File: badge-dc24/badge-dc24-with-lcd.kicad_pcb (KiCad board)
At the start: 2 copper layers, 22 parts, among them P1 CONN_01X02, U1 ESP-12E, U2 TSOP38238, U3 74HC595

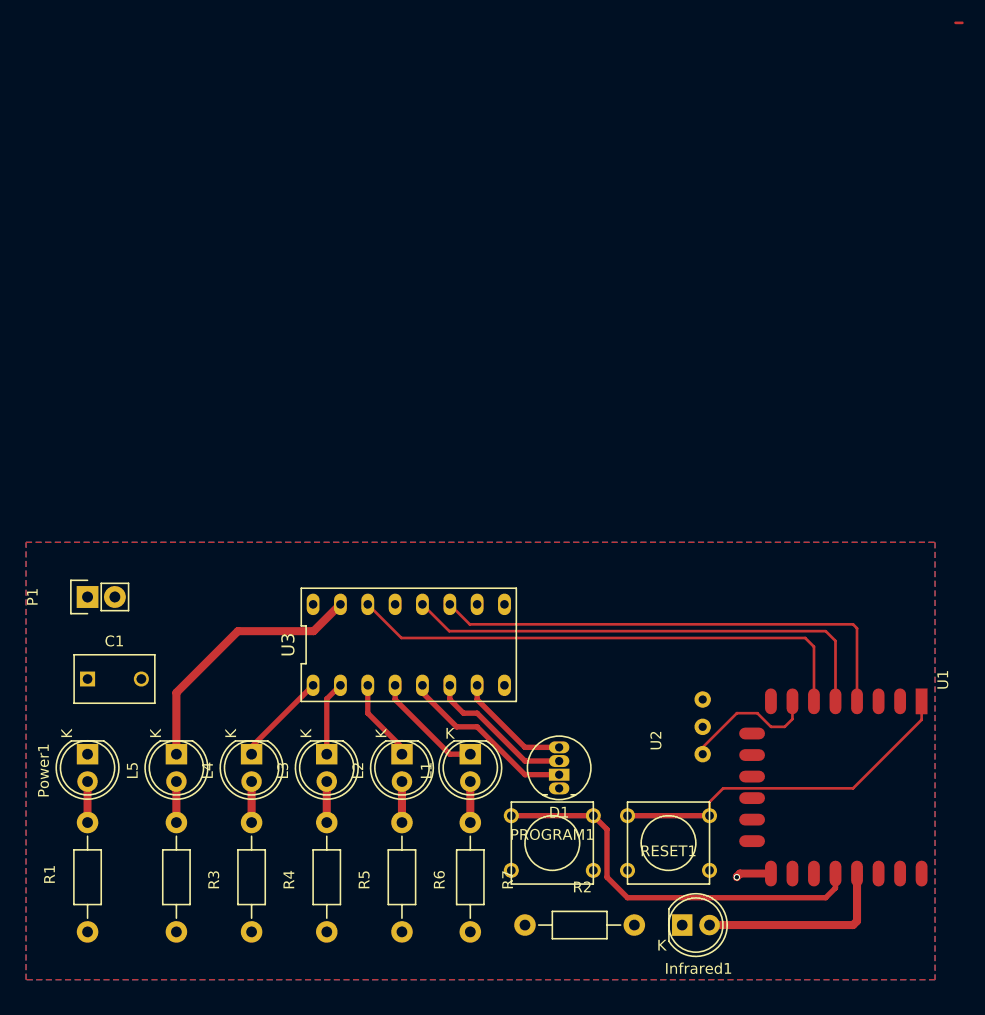
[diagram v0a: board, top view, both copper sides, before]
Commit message: SMD fir some components
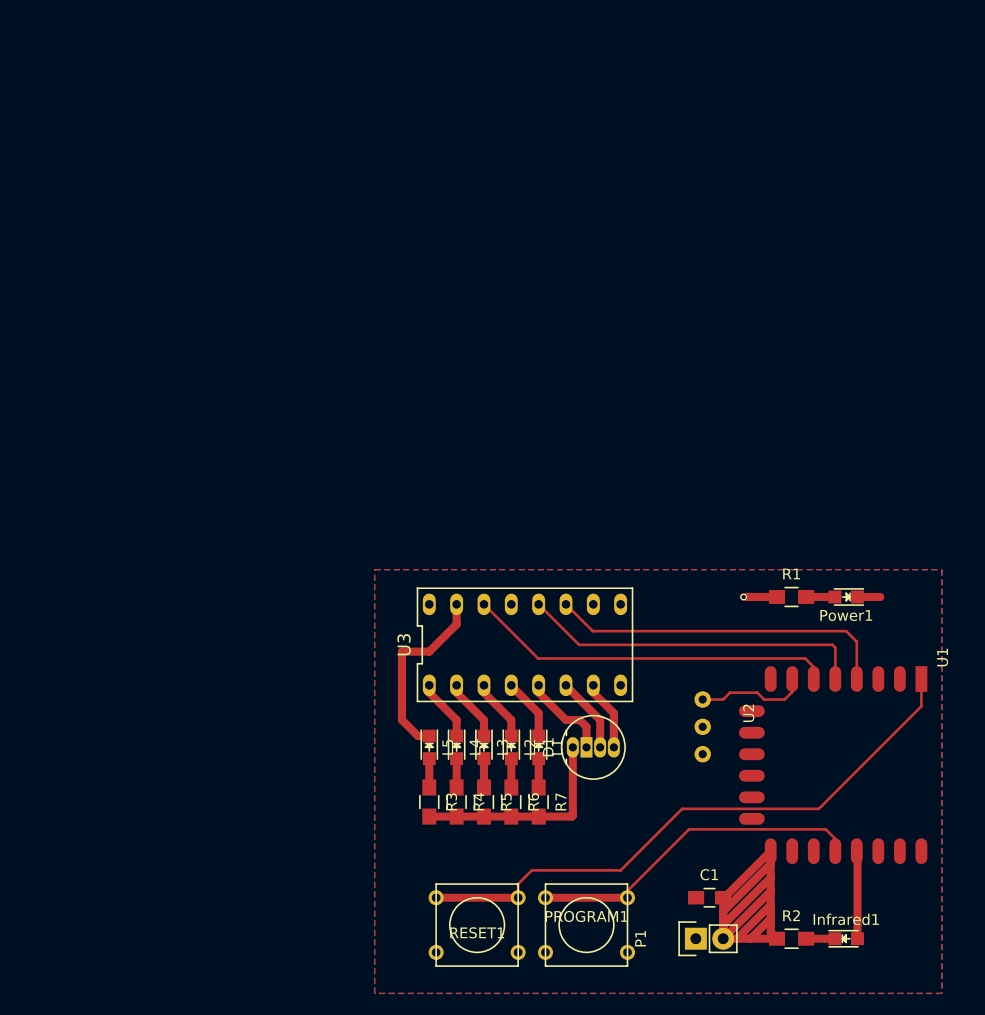
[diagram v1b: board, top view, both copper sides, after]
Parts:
- C1: footprint Capacitors_ThroughHole:C_Disc_D7.5_P5 -> Capacitors_SMD:C_0805_HandSoldering
- Infrared1, L1, L2, L3, L4, L5, Power1: footprint LEDs:LED-5MM -> LEDs:LED_0805
- R1, R2, R3, R4, R5, R6, R7: footprint Resistors_ThroughHole:Resistor_Horizontal_RM10mm -> Resistors_SMD:R_0805_HandSoldering
- moved R1 72.4 mm to (132.7, 78.1), turned to 0 degrees
- moved Power1 72.0 mm to (137.8, 78.1), turned to 180 degrees
- moved P1 64.8 mm to (123.8, 109.9)
- moved C1 61.3 mm to (125.1, 106.0)
- moved R2 24.8 mm to (132.7, 109.9)
- moved R3 23.6 mm to (99.1, 97.2)
- moved L5 23.5 mm to (99.1, 92.1)
- moved RESET1 19.3 mm to (103.5, 108.6)
- moved R4 19.1 mm to (101.6, 97.2)
- moved L4 19.1 mm to (101.6, 92.1)
- moved Infrared1 15.3 mm to (137.8, 109.9)
- moved R5 14.7 mm to (104.1, 97.2)
- moved L3 14.6 mm to (104.1, 92.1)
- moved U3 10.8 mm to (108.0, 82.5)
- moved R6 10.3 mm to (106.7, 97.2)
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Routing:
- net GND: track 3.33 -> 79.0 mm
- net Net-(RESET1-Pad2): track 33.6 -> 55.7 mm
- net Net-(U1-Pad6): track 49.0 -> 34.2 mm
- net Net-(U1-Pad4): track 45.5 -> 31.9 mm
- net Net-(U1-Pad5): track 45.4 -> 32.1 mm
- net Net-(Infrared1-Pad2): track 18.7 -> 8.16 mm
- net Net-(D1-Pad2): track 16.5 -> 8.35 mm
- net Net-(L5-Pad1): track 24.4 -> 17.5 mm
- net Net-(D1-Pad3): track 13.8 -> 7.08 mm
- net Net-(PROGRAM1-Pad1): track 37.6 -> 31.4 mm
- net Net-(L1-Pad1): track 10.4 -> 5.77 mm
- net Net-(D1-Pad4): track 10.8 -> 6.55 mm
- net Net-(L4-Pad1): track 8.77 -> 5.77 mm
- net Net-(Infrared1-Pad1): track 0.00 -> 2.68 mm
- net Net-(U1-Pad7): track 12.8 -> 10.3 mm
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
